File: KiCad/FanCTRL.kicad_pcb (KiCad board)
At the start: 2 copper layers, 27.2 x 38.6 mm, 20 parts, among them J201 Conn_01x04_Pin, J202 Conn_01x04_Pin, Q301 BSS138, Q401 BSS138, U201 AP2112K-3.3, U202 STM32G030F6Px

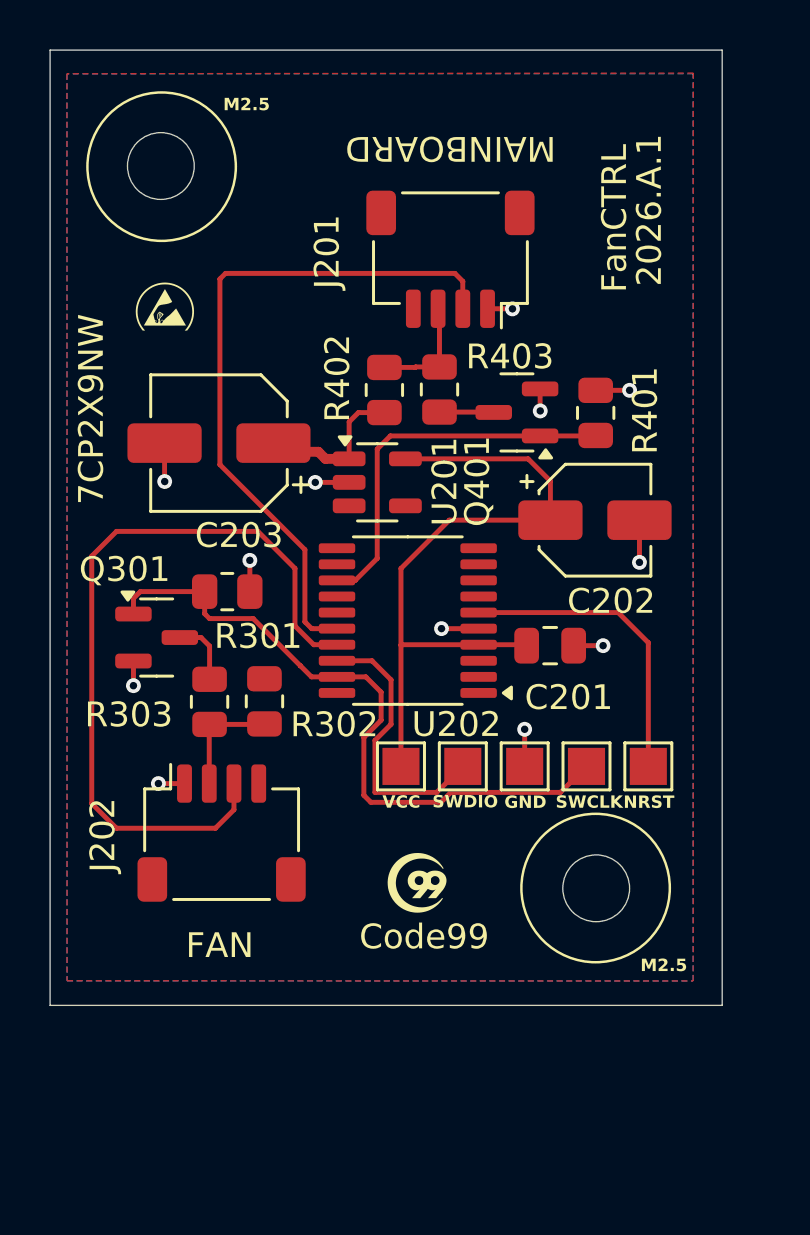
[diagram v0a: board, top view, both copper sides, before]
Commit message: Added and edited some Texts in Schematic and Board
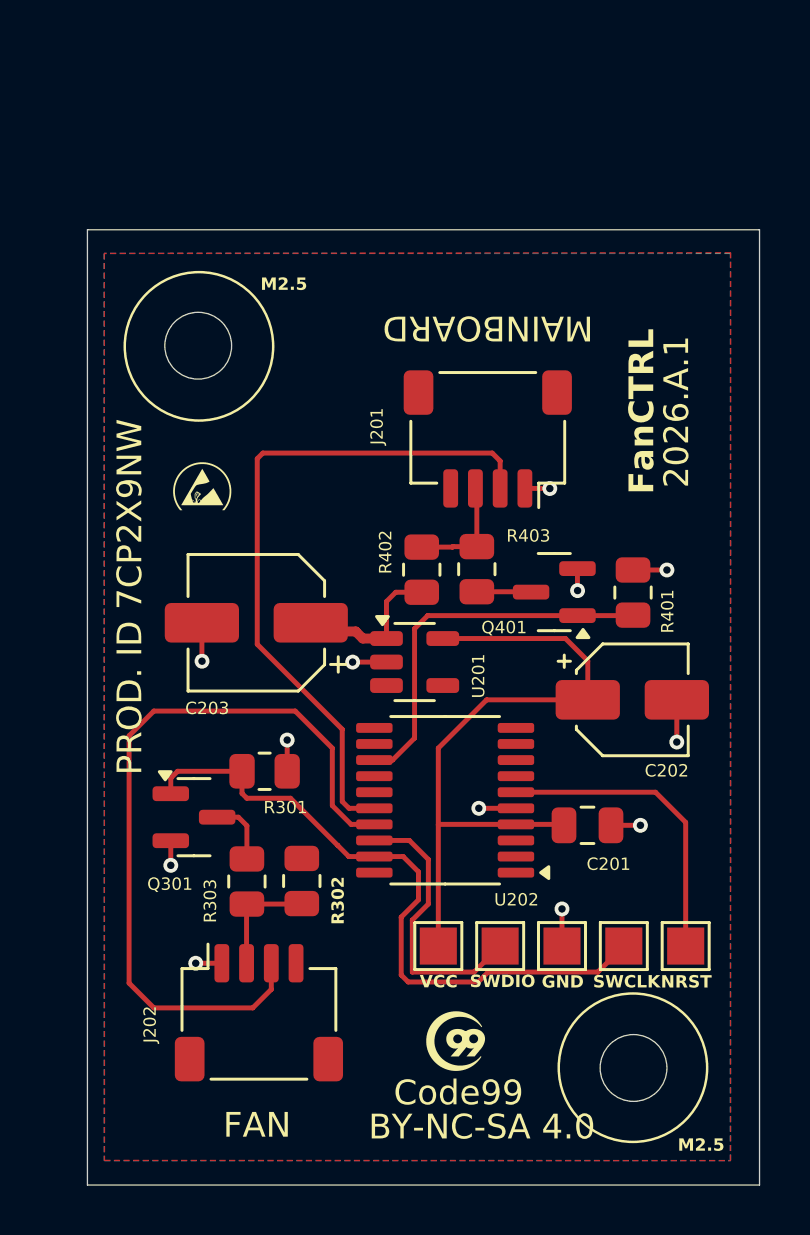
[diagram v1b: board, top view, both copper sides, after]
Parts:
- moved R302 7.42 mm to (140.0, 102.6)
- moved C201 7.42 mm to (151.5, 100.4)
- moved C202 7.42 mm to (153.4, 95.3)
- moved C203 7.42 mm to (138.2, 92.2)
- moved H201 7.42 mm to (153.0, 105.3)
- moved H202 7.42 mm to (145.5, 105.3)
- moved H203 7.42 mm to (150.5, 105.3)
- moved H204 7.42 mm to (155.5, 105.3)
- moved H205 7.42 mm to (148.0, 105.3)
- moved J201 7.42 mm to (147.5, 84.8)
- moved J202 7.42 mm to (138.3, 108.0)
- moved Q301 7.42 mm to (135.6, 100.1)
- moved R301 7.42 mm to (138.5, 98.2)
- moved R401 7.42 mm to (153.4, 91.0)
- moved R402 7.42 mm to (144.8, 90.0)
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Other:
- board text added: "BY-NC-SA 4.0"
- board text added: "PROD. ID 7CP2X9NW"
- board text removed: "7CP2X9NW"
